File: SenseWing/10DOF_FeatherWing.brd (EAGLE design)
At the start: 22.9 x 50.8 mm, 16 parts

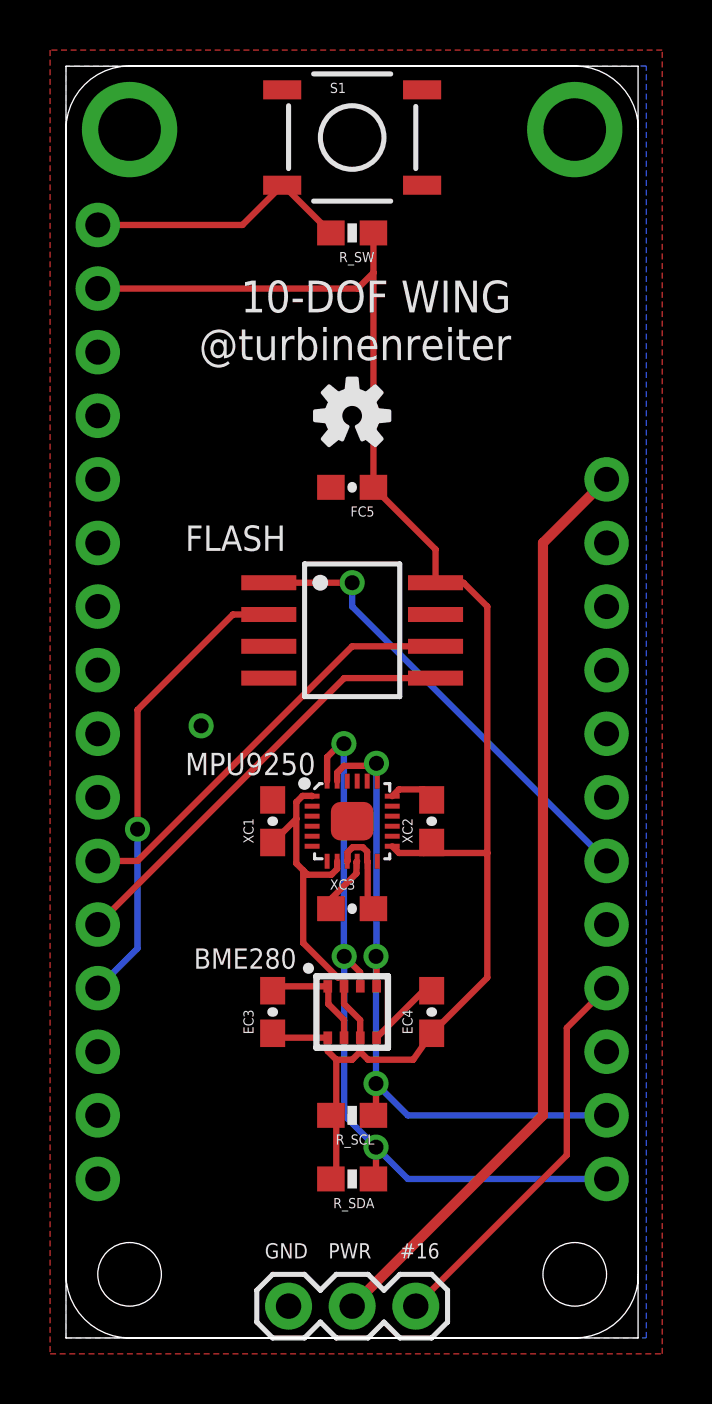
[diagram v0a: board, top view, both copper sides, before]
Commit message: added v5 SenseWing
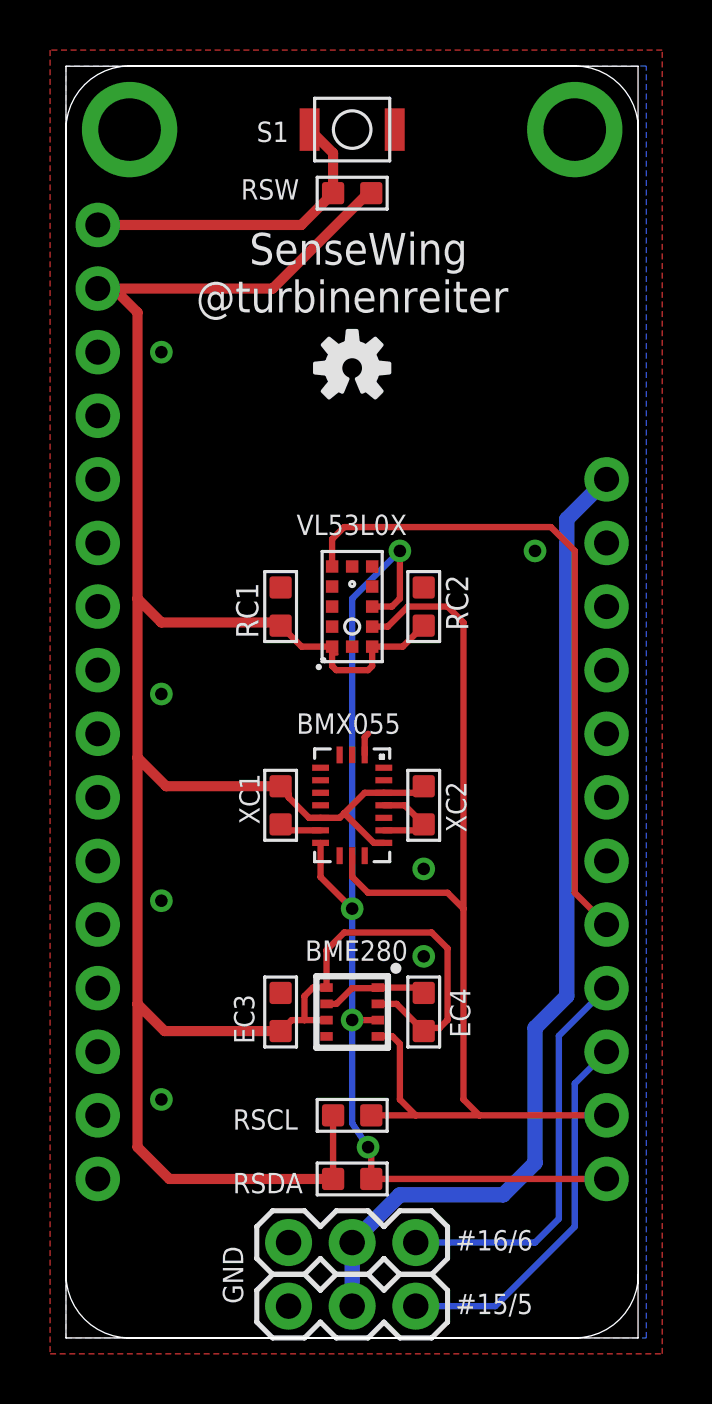
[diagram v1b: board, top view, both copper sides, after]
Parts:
- removed FC5, XC3: 0.1uF, SparkFun-Capacitors:0603-CAP
- removed FLASH: S25FL127SABMFI101, memory-spansion:SO08-S2A
- removed MPU9250: MPU-9250, Seeed-OPL-sensor:QFN24G-0.4-3X3MM
- removed R_SCL, R_SDA: 4.7K, SparkFun-Resistors:0603-RES
- removed R_SW: 10K, SparkFun-Resistors:0603-RES
- added BMX055: X-IO_BMX055, BMX055 Breakout:X-IO_BMX055
- added RC1: 100nf, Seeed-OPL-Capacitor:C0603
- added RC2: 4.7uf, Seeed-OPL-Capacitor:C0603
- added RSCL, RSDA: 4.7K, Seeed-OPL-Resistor:R0603
- added RSW: 10K, Seeed-OPL-Resistor:R0603
- added SRV_H2: (no value), SparkFun-Connectors:1X03
- added U$1: VL53L0X, VL53L0X:VL53L0X
- EC3, EC4, XC1, XC2: value 0.1uF -> 100nf; device SparkFun-Capacitors:0603-CAP -> Seeed-OPL-Capacitor:C0603
- S1: value SWITCH-MOMENTARY-2SMD -> B3U-1000P; device SparkFun-Electromechanical:TACTILE-SWITCH-SMD -> Seeed-OPL-Button:SW2-SMD-3.0X2.5X1.2+0.4MM
- moved SRV_H1 2.54 mm to (8.89, 3.81)
- moved LOGO1 1.91 mm to (11.4, 38.7)
- moved XC2 0.71 mm to (14.3, 21.3), turned to 0 degrees
- moved XC1 0.71 mm to (8.57, 21.3), turned to 0 degrees
- moved EC4 0.32 mm to (14.3, 13.0), turned to 180 degrees
- moved EC3 0.32 mm to (8.57, 13.0), turned to 180 degrees
- moved S1 0.32 mm to (11.4, 48.3), turned to 180 degrees
- turned BME280 to 0 degrees
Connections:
- removed net N$2: MPU9250.10, XC3.1
- new net AI1: BMX055.19
- new net AI2: BMX055.1
- new net GI1: BMX055.14
- new net GI2: BMX055.15
- new net MDR: BMX055.2
- new net MI: BMX055.10
- net #0_RED_BL: now also U$1.5
- net #15_PD_BL: no longer FLASH.1
- net #2_BLUE_PU_BL: now also SRV_H2.3
- net 3.3V: now also BMX055.13, BMX055.3, BMX055.7, RC1.1, RC2.2, RSCL.2, RSDA.2, RSW.1, U$1.1, U$1.11; no longer FC5.1, FLASH.8, MPU9250.1, MPU9250.13, MPU9250.8, R_SCL.2, R_SDA.2, R_SW.1
- net GND: now also BMX055.12, BMX055.17, BMX055.20, BMX055.4, BMX055.6, RC1.2, RC2.1, SRV_H2.1, U$1.12, U$1.2, U$1.3, U$1.4, U$1.6; no longer FC5.2, FLASH.4, MPU9250.11, MPU9250.18, MPU9250.9, XC3.2
- net MISO: no longer FLASH.2
- net MOSI: no longer FLASH.5
- net SCK: no longer FLASH.6
- net SCL: now also BMX055.9, RSCL.1, U$1.10; no longer MPU9250.23, R_SCL.1
- net SDA: now also BMX055.11, RSDA.1, U$1.9; no longer MPU9250.24, R_SDA.1
- net SW1: now also RSW.2, S1.2; no longer R_SW.2, S1.3
- net VBAT: now also SRV_H2.2
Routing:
- net 3.3V: track 80.2 -> 111.2 mm
- net #0_RED_BL: track 0.00 -> 26.8 mm
- net #15_PD_BL: track 18.7 -> 0.00 mm, vias 1 -> 0
- net MISO: track 18.6 -> 0.00 mm, vias 1 -> 0
- net MOSI: track 17.6 -> 0.00 mm
- net SCK: track 17.0 -> 0.00 mm
- net SCL: track 27.1 -> 43.5 mm, vias 3 -> 0
- net #2_BLUE_PU_BL: track 0.00 -> 15.2 mm
- net SDA: track 31.0 -> 42.8 mm, vias 3 -> 4
- net GND: track 13.3 -> 10.4 mm, vias 1 -> 7
- net VBAT: track 37.2 -> 39.6 mm
- net N$2: track 2.33 -> 0.00 mm
- net SW1: track 10.8 -> 12.9 mm
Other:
- board text added: "#15/5"
- board text added: "#16/6"
- board text added: "SenseWing @turbinenreiter"
- board text added: "VL53L0X"
- board text removed: "#16"
- board text removed: "10-DOF WING @turbinenreiter"
- board text removed: "PWR"
